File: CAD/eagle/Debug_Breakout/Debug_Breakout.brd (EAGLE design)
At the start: 26.7 x 39.4 mm, 16 parts, among them Q1 CM1213A-02SR, Q2 CM1213A-02SR

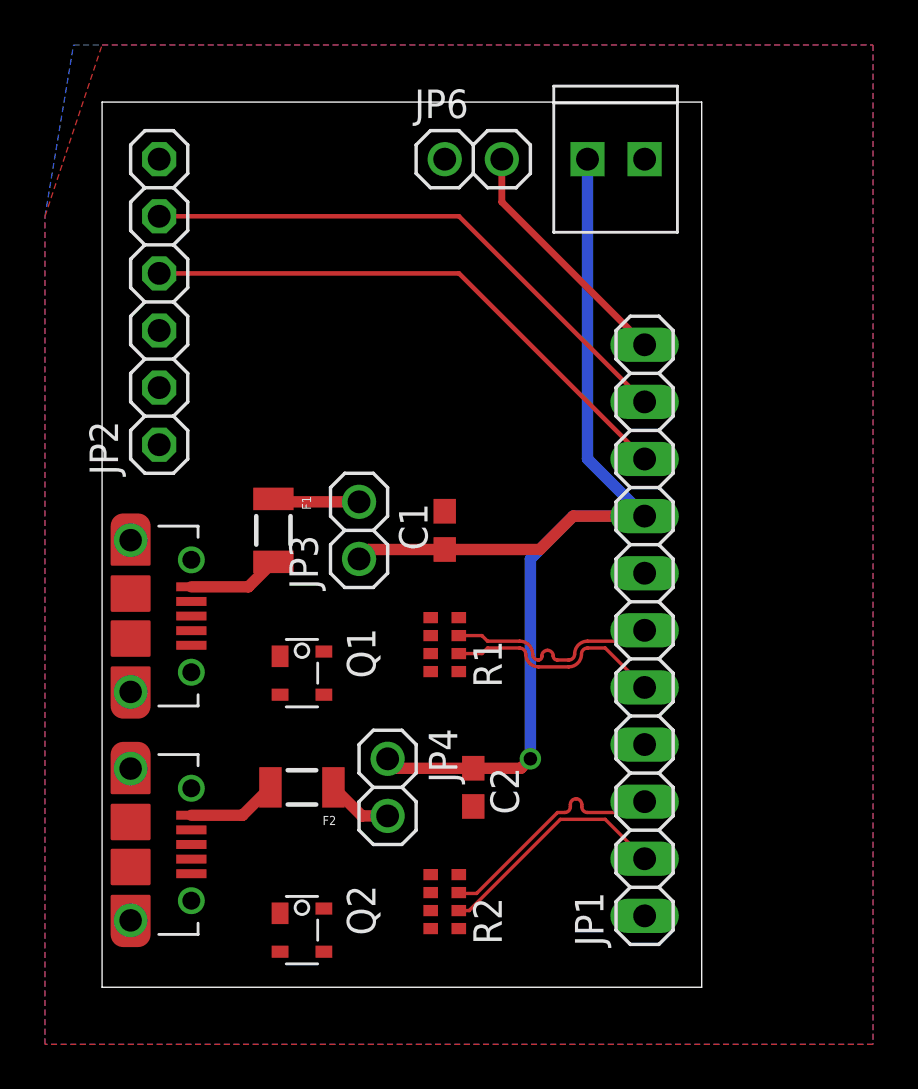
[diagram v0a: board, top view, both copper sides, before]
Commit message: Finished STAR debug board.
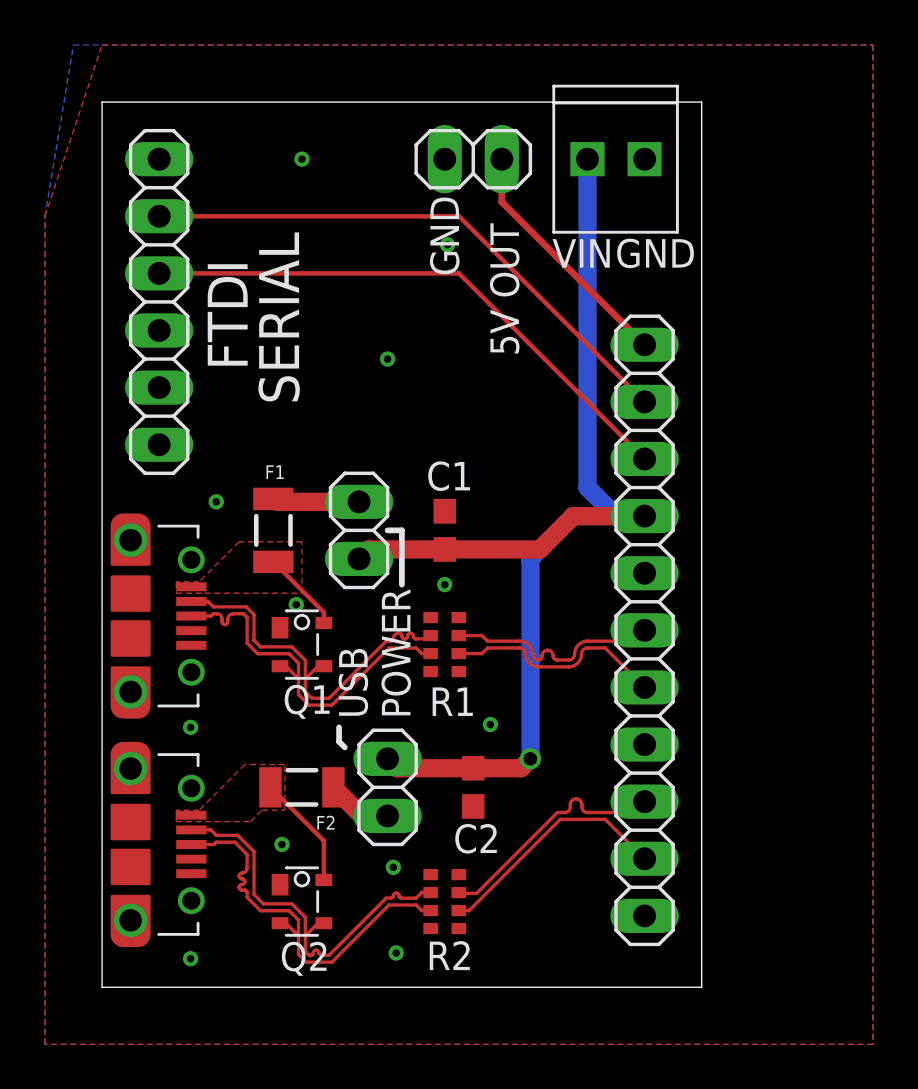
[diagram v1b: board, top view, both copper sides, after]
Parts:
- added U$1: SSL.3IN_SILK, images:SSL_SILK_.3IN
- added U$2: STAR, images:STAR_.3IN
- moved Q2 1.27 mm to (8.89, 3.81)
- moved Q1 1.27 mm to (8.89, 15.2)
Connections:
- removed net N$1: MCU.3, Q1.P$3, R1.7
- removed net N$2: MCU.2, Q1.P$2, R1.6
- removed net N$3: PI.3, Q2.P$3, R2.7
- removed net N$4: PI.2, Q2.P$2, R2.6
- removed net N$6: PI.5, PI.S1, PI.S2, PI.S3, PI.S4, Q2.P$1
- removed net N$7: MCU.5, MCU.S1, MCU.S2, MCU.S3, MCU.S4, Q1.P$1
- new net MCU_D_N: MCU.2, Q1.P$3, R1.6
- new net MCU_D_P: MCU.3, Q1.P$2, R1.7
- new net PICONN_D_N: PI.2, Q2.P$3, R2.6
- new net PICONN_D_P: PI.3, Q2.P$2, R2.7
- net GND: now also MCU.5, MCU.S1, MCU.S2, MCU.S3, MCU.S4, PI.5, PI.S1, PI.S2, PI.S3, PI.S4, Q1.P$1, Q2.P$1
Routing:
- net PICONN_D_P: track 0.00 -> 17.7 mm
- net PICONN_D_N: track 0.00 -> 17.6 mm
- net MCU_D_P: track 0.00 -> 16.6 mm
- net MCU_D_N: track 0.00 -> 16.5 mm
- net N$5: track 4.03 -> 5.10 mm
- net VCC: track 51.9 -> 51.3 mm
- added copper zone on layer 1, net N$5
- added copper zone on layer 1, net N$8
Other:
- board text added: "5V OUT"
- board text added: "FTDI"
- board text added: "GND"
- board text added: "PI USB"
- board text added: "SERIAL"
- board text added: "STAR DEBUG BOARD"
- board text added: "STARDUINO USB"
- board text added: "USB POWER"
- board text added: "VIN"

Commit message: ESB traces and breakout 15 pin labels
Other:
- board text added: "5V"
- board text added: "MCU+"
- board text added: "MCU-"
- board text added: "PI+"
- board text added: "PI-"
- board text added: "RX"
- board text added: "TX"
- board text added: "VCC"
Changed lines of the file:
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@@
 <?xml version="1.0" encoding="utf-8"?>
 <!DOCTYPE eagle SYSTEM "eagle.dtd">
-<eagle version="7.7.0">
+<eagle version="6.5.0">
 <drawing>
 <settings>
@@
 <wire x1="10.541" y1="11.557" x2="10.541" y2="10.922" width="0.254" layer="21"/>
 <wire x1="10.541" y1="10.922" x2="10.795" y2="10.668" width="0.254" layer="21"/>
+<text x="20.32" y="27.94" size="1.27" layer="21">5V</text>
+<text x="19.05" y="20.32" size="1.27" layer="21">VCC</text>
+<text x="20.32" y="22.86" size="1.27" layer="21">TX</text>
+<text x="20.32" y="25.4" size="1.27" layer="21">RX</text>
+<text x="19.05" y="17.78" size="1.27" layer="21">GND</text>
+<text x="17.78" y="12.7" size="1.27" layer="21">MCU+</text>
+<text x="17.78" y="15.24" size="1.27" layer="21">MCU-</text>
+<text x="19.05" y="10.16" size="1.27" layer="21">GND</text>
+<text x="19.05" y="7.62" size="1.27" layer="21">PI-</text>
+<text x="19.05" y="5.08" size="1.27" layer="21">PI+</text>
+<text x="19.05" y="2.54" size="1.27" layer="21">GND</text>
 </plain>
 <attributes>
@@
 <pass name="Default">
 <param name="RoutingGrid" value="50mil"/>
-<param name="AutoGrid" value="1"/>
-<param name="Efforts" value="0"/>
-<param name="TopRouterVariant" value="1"/>
 <param name="tpViaShape" value="round"/>
-<param name="PrefDir.1" value="a"/>
+<param name="PrefDir.1" value="|"/>
 <param name="PrefDir.2" value="0"/>
 <param name="PrefDir.3" value="0"/>
@@
 <param name="PrefDir.14" value="0"/>
 <param name="PrefDir.15" value="0"/>
-<param name="PrefDir.16" value="a"/>
+<param name="PrefDir.16" value="-"/>
 <param name="cfVia" value="8"/>
 <param name="cfNonPref" value="5"/>
